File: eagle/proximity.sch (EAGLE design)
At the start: 13 parts

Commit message: added PCB file
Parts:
- removed DSPL: (no value), con-amp-quick:MA16
- removed PROX1, PROX2, PROX3: (no value), con-lstb:MA04-1
- removed RPI1: (no value), con-lstb:MA13-2
- added JP1: (no value), pinhead:PINHD-2X13
- added JP2: (no value), pinhead:PINHD-1X16
- added JP3, JP4, JP5: (no value), pinhead:PINHD-1X4
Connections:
- removed net 0: DSPL.3, PROX1.1, PROX2.1, PROX3.1, R1.2, R3.1, R5.2, R7.2, RPI1.6
- new net +5V: JP1.2, JP3.4, JP4.4, JP5.4
- new net GND: JP1.6, JP2.3, JP3.1, JP4.1, JP5.1, R1.2, R3.1, R5.2, R7.2
- net DISPL_DB4: now also JP1.19, JP2.13; no longer DSPL.13, RPI1.19
- net DISPL_DB5: now also JP1.21, JP2.14; no longer DSPL.14, RPI1.21
- net DISPL_DB6: now also JP1.23, JP2.15; no longer DSPL.15, RPI1.23
- net DISPL_DB7: now also JP1.22, JP2.16; no longer DSPL.16, RPI1.22
- net DISPL_E: now also JP1.18, JP2.8; no longer DSPL.8, RPI1.18
- net DISPL_RS: now also JP1.16, JP2.6; no longer DSPL.6, RPI1.16
- net DISPL_RW: now also JP2.7; no longer DSPL.7
- net N$1: now also JP3.2; no longer PROX1.2
- net N$2: now also JP4.2; no longer PROX2.2
- net N$3: now also JP5.2; no longer PROX3.2
- net PR1_ECHO: now also JP1.13; no longer RPI1.13
- net PR1_TRIGGER: now also JP1.11, JP3.3; no longer PROX1.3, RPI1.11
- net PR2_ECHO: now also JP1.5; no longer RPI1.5
- net PR2_TRIGGER: now also JP1.3, JP4.3; no longer PROX2.3, RPI1.3
- net PR3_ECHO: now also JP1.15; no longer RPI1.15
- net PR3_TRIGGER: now also JP1.7, JP5.3; no longer PROX3.3, RPI1.7
- net VCC: now also JP2.4; no longer DSPL.4, PROX1.4, PROX2.4, PROX3.4, RPI1.2
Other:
- moved on the sheet: R4, R5, R6, R7

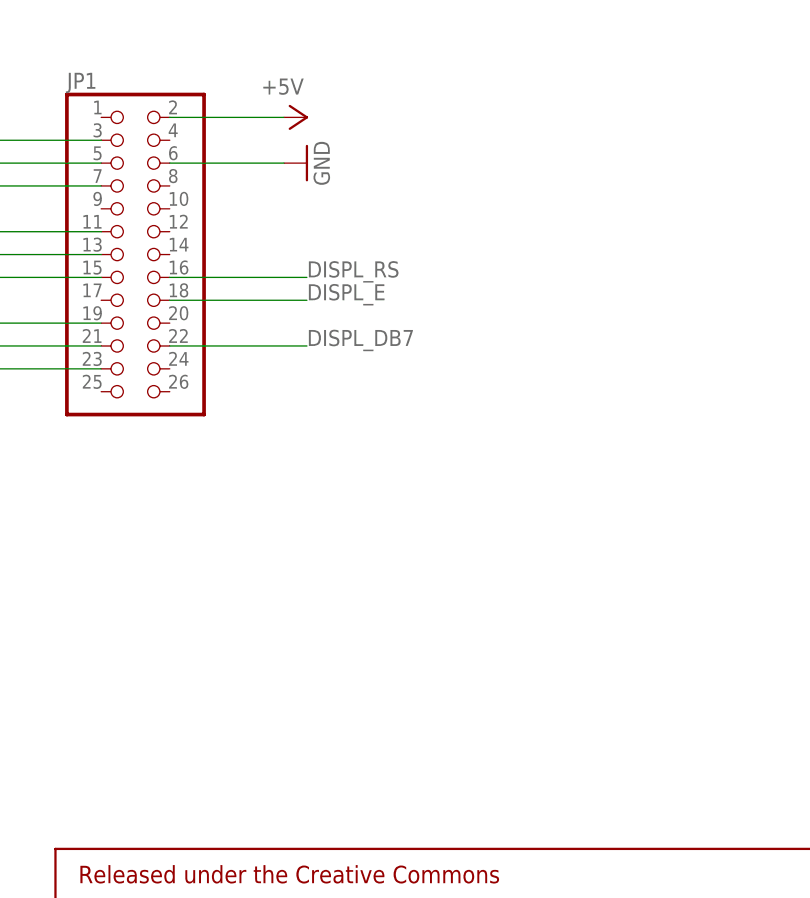
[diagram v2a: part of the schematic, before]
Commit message: added USB to serial to schematic
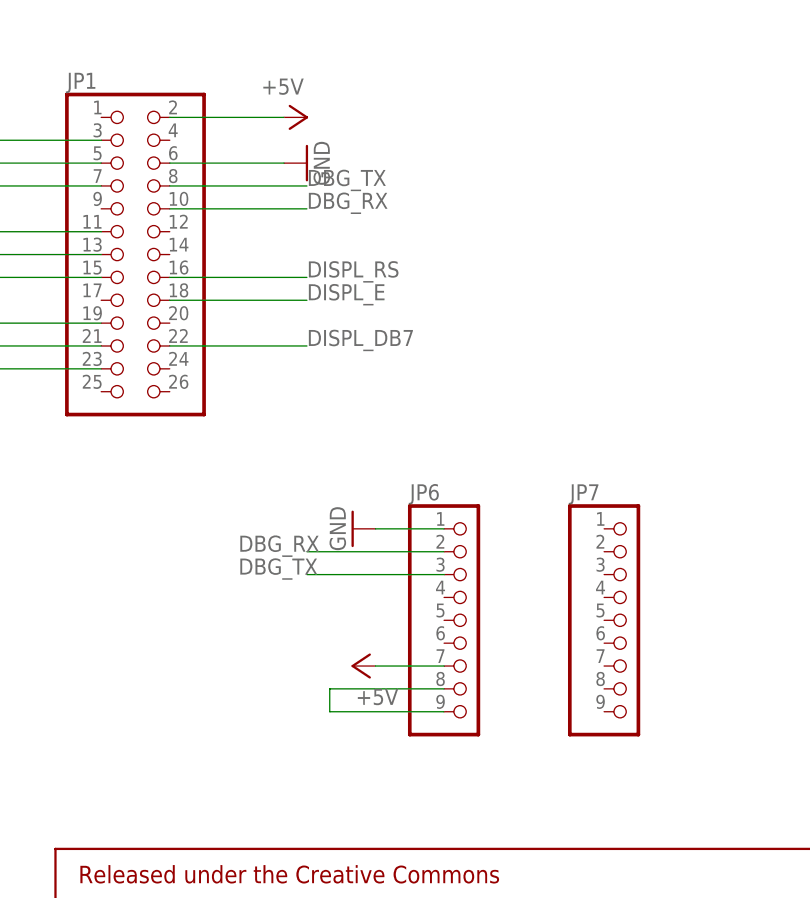
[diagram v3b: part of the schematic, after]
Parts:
- added JP6, JP7: (no value), pinhead:PINHD-1X9
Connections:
- new net DBG_RX: JP1.10, JP6.2
- new net DBG_TX: JP1.8, JP6.3
- new net N$10: JP6.8, JP6.9
- net +5V: now also JP6.7
- net GND: now also JP6.1
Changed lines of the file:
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@@
 <?xml version="1.0" encoding="utf-8"?>
 <!DOCTYPE eagle SYSTEM "eagle.dtd">
-<eagle version="8.4.0">
+<eagle version="8.4.1">
 <drawing>
 <settings>
@@
 <part name="GND8" library="supply1" library_urn="urn:adsk.eagle:library:371" deviceset="GND" device=""/>
 <part name="GND9" library="supply1" library_urn="urn:adsk.eagle:library:371" deviceset="GND" device=""/>
+<part name="JP6" library="pinhead" library_urn="urn:adsk.eagle:library:325" deviceset="PINHD-1X9" device="" package3d_urn="urn:adsk.eagle:package:22483/1"/>
+<part name="JP7" library="pinhead" library_urn="urn:adsk.eagle:library:325" deviceset="PINHD-1X9" device="" package3d_urn="urn:adsk.eagle:package:22483/1"/>
+<part name="P+2" library="supply1" library_urn="urn:adsk.eagle:library:371" deviceset="+5V" device=""/>
+<part name="GND10" library="supply1" library_urn="urn:adsk.eagle:library:371" deviceset="GND" device=""/>
 </parts>
 <sheets>
@@
 <instance part="GND8" gate="1" x="134.62" y="200.66" rot="R270"/>
 <instance part="GND9" gate="1" x="160.02" y="210.82" rot="R270"/>
+<instance part="JP6" gate="A" x="137.16" y="106.68"/>
+<instance part="JP7" gate="A" x="154.94" y="106.68"/>
+<instance part="P+2" gate="1" x="124.46" y="101.6" rot="R90"/>
+<instance part="GND10" gate="1" x="124.46" y="116.84" rot="R270"/>
 </instances>
 <busses>
@@
 <pinref part="GND9" gate="1" pin="GND"/>
 </segment>
+<segment>
+<pinref part="JP6" gate="A" pin="1"/>
+<wire x1="134.62" y1="116.84" x2="127" y2="116.84" width="0.1524" layer="91"/>
+<pinref part="GND10" gate="1" pin="GND"/>
+</segment>
 </net>
 <net name="+5V" class="0">
@@
 <pinref part="P+5" gate="1" pin="+5V"/>
 <wire x1="104.14" y1="162.56" x2="116.84" y2="162.56" width="0.1524" layer="91"/>
+</segment>
+<segment>
+<pinref part="JP6" gate="A" pin="7"/>
+<wire x1="134.62" y1="101.6" x2="127" y2="101.6" width="0.1524" layer="91"/>
+<pinref part="P+2" gate="1" pin="+5V"/>
 </segment>
 </net>
@@
 </segment>
 </net>
+<net name="N$10" class="0">
+<segment>
+<pinref part="JP6" gate="A" pin="8"/>
+<wire x1="134.62" y1="99.06" x2="121.92" y2="99.06" width="0.1524" layer="91"/>
+<wire x1="121.92" y1="99.06" x2="121.92" y2="96.52" width="0.1524" layer="91"/>
+<pinref part="JP6" gate="A" pin="9"/>
+<wire x1="121.92" y1="96.52" x2="134.62" y2="96.52" width="0.1524" layer="91"/>
+</segment>
+</net>
+<net name="DBG_TX" class="0">
+<segment>
+<pinref part="JP1" gate="A" pin="8"/>
+<wire x1="104.14" y1="154.94" x2="119.38" y2="154.94" width="0.1524" layer="91"/>
+<label x="119.38" y="154.94" size="1.778" layer="95"/>
+</segment>
+<segment>
+<pinref part="JP6" gate="A" pin="3"/>
+<wire x1="134.62" y1="111.76" x2="119.38" y2="111.76" width="0.1524" layer="91"/>
+<label x="111.76" y="111.76" size="1.778" layer="95"/>
+</segment>
+</net>
+<net name="DBG_RX" class="0">
+<segment>
+<pinref part="JP1" gate="A" pin="10"/>
+<wire x1="104.14" y1="152.4" x2="119.38" y2="152.4" width="0.1524" layer="91"/>
+<label x="119.38" y="152.4" size="1.778" layer="95"/>
+</segment>
+<segment>
+<pinref part="JP6" gate="A" pin="2"/>
+<wire x1="134.62" y1="114.3" x2="119.38" y2="114.3" width="0.1524" layer="91"/>
+<label x="111.76" y="114.3" size="1.778" layer="95"/>
+</segment>
+</net>

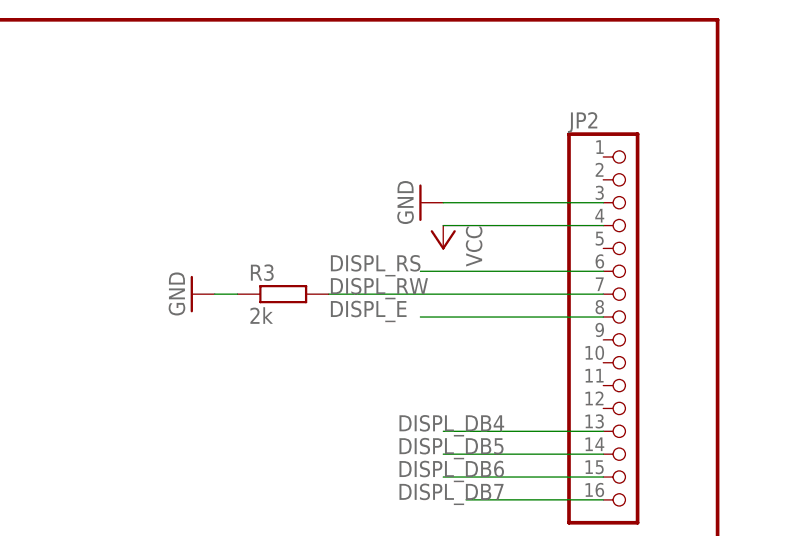
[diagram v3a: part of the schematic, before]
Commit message: echo IRQ is shared because it is used by different gpio pins
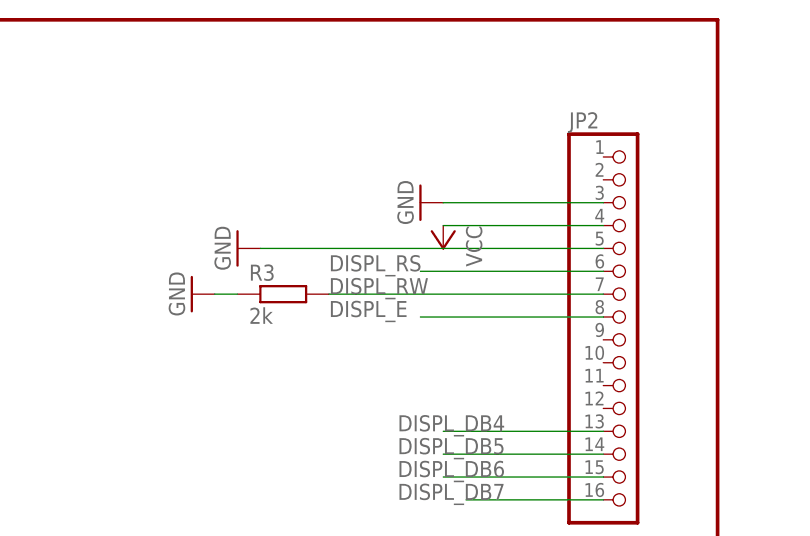
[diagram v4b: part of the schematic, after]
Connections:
- net GND: now also JP2.5
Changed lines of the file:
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@@
 <part name="P+2" library="supply1" library_urn="urn:adsk.eagle:library:371" deviceset="+5V" device=""/>
 <part name="GND10" library="supply1" library_urn="urn:adsk.eagle:library:371" deviceset="GND" device=""/>
+<part name="GND11" library="supply1" library_urn="urn:adsk.eagle:library:371" deviceset="GND" device=""/>
 </parts>
 <sheets>
@@
 <instance part="P+2" gate="1" x="124.46" y="101.6" rot="R90"/>
 <instance part="GND10" gate="1" x="124.46" y="116.84" rot="R270"/>
+<instance part="GND11" gate="1" x="139.7" y="205.74" rot="R270"/>
 </instances>
 <busses>
@@
 <pinref part="GND10" gate="1" pin="GND"/>
 </segment>
-</net>
+<segment>
+<pinref part="GND11" gate="1" pin="GND"/>
+<pinref part="JP2" gate="A" pin="5"/>
+<wire x1="142.24" y1="205.74" x2="180.34" y2="205.74" width="0.1524" layer="91"/>
+</segment>
+</net>
